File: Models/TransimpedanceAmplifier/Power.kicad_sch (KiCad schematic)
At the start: 4 parts

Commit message: Save progress
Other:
- note added: "TODO: Purchase links for regulators Purchase links for new trimpots (Y variant) Footprints for 0805 capacitors Purchase links & footprints for Schottky diodes Finalize all decoupling networks"
- note removed: "TODO: Purchase links for regulators Purchase links for new trimpots (Y variant)"
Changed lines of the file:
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@@
 		)
 	)
-	(text "TODO:\nPurchase links for regulators\nPurchase links for new trimpots (Y variant)"
+	(text "TODO:\nPurchase links for regulators\nPurchase links for new trimpots (Y variant)\nFootprints for 0805 capacitors\nPurchase links & footprints for Schottky diodes\nFinalize all decoupling networks"
 		(exclude_from_sim no)
-		(at 107.442 61.976 0)
+		(at 102.616 56.896 0)
 		(effects
 			(font

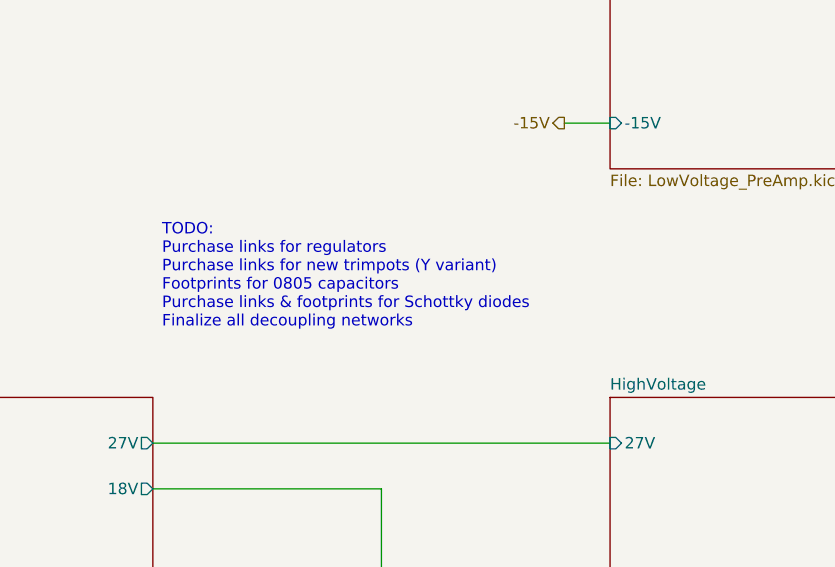
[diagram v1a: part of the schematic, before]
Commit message: Overhauled the purchase links for regulators and trimpots
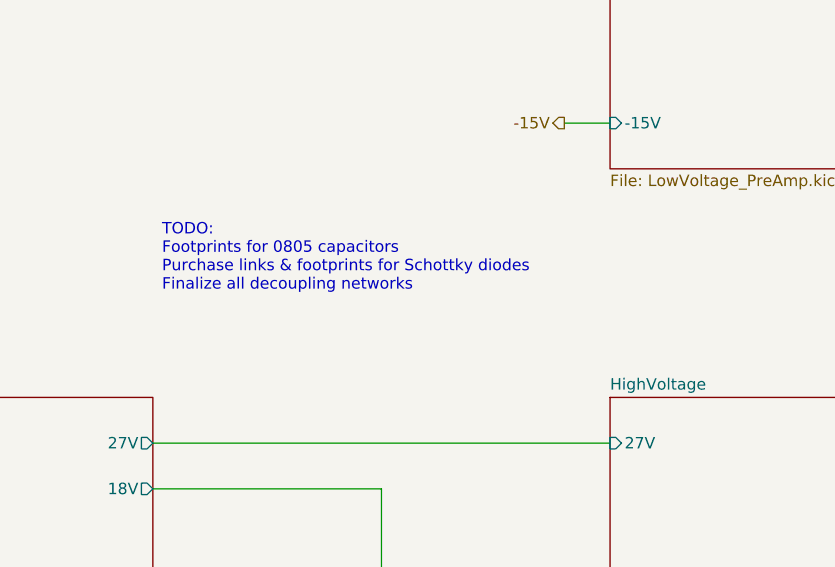
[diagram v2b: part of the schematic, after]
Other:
- note added: "TODO: Footprints for 0805 capacitors Purchase links & footprints for Schottky diodes Finalize all decoupling networks"
- note removed: "TODO: Purchase links for regulators Purchase links for new trimpots (Y variant) Footprints for 0805 capacitors Purchase links & footprints for Schottky diodes Finalize all decoupling networks"
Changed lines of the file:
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@@
 		)
 	)
-	(text "TODO:\nPurchase links for regulators\nPurchase links for new trimpots (Y variant)\nFootprints for 0805 capacitors\nPurchase links & footprints for Schottky diodes\nFinalize all decoupling networks"
+	(text "TODO:\nFootprints for 0805 capacitors\nPurchase links & footprints for Schottky diodes\nFinalize all decoupling networks"
 		(exclude_from_sim no)
 		(at 102.616 56.896 0)

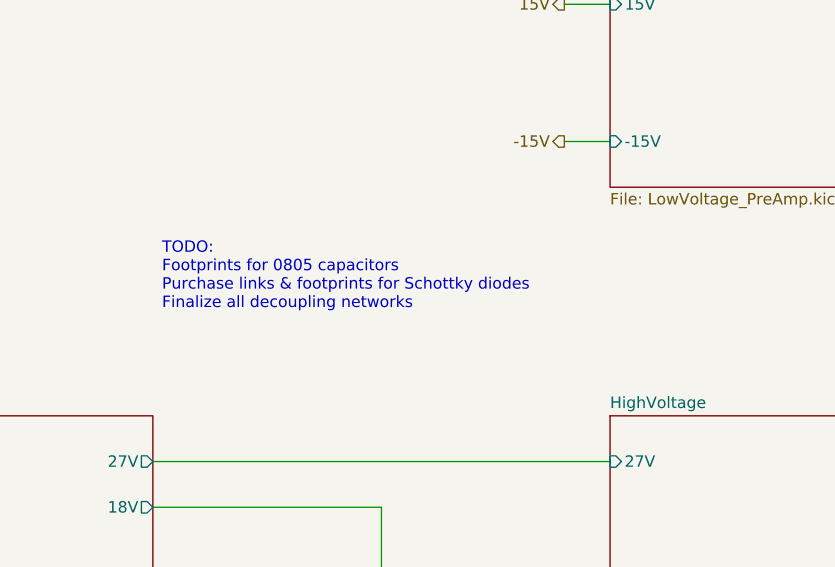
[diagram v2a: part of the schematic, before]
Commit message: Finished the footprint for 0805 capacitors
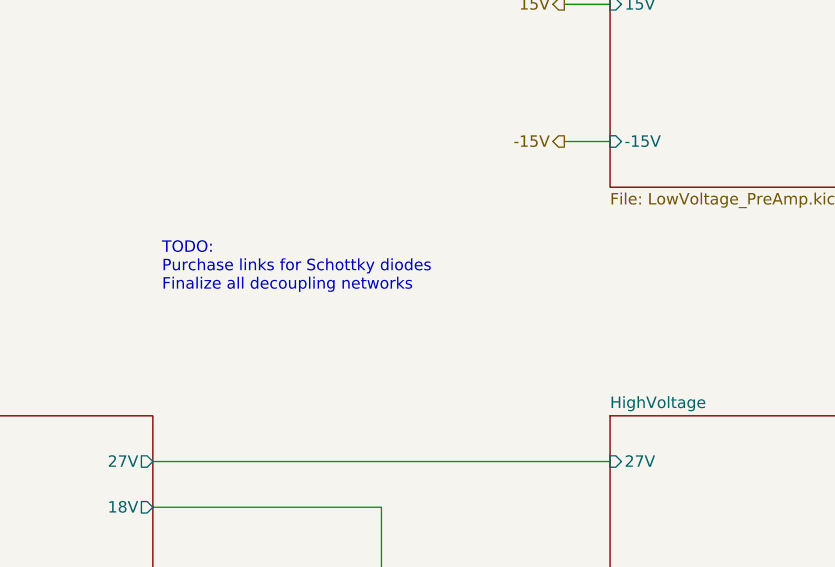
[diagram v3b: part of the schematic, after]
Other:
- note added: "TODO: Purchase links for Schottky diodes Finalize all decoupling networks"
- note removed: "TODO: Footprints for 0805 capacitors Purchase links & footprints for Schottky diodes Finalize all decoupling networks"
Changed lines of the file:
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@@
 		)
 	)
-	(text "TODO:\nFootprints for 0805 capacitors\nPurchase links & footprints for Schottky diodes\nFinalize all decoupling networks"
+	(text "TODO:\nPurchase links for Schottky diodes\nFinalize all decoupling networks"
 		(exclude_from_sim no)
 		(at 102.616 56.896 0)

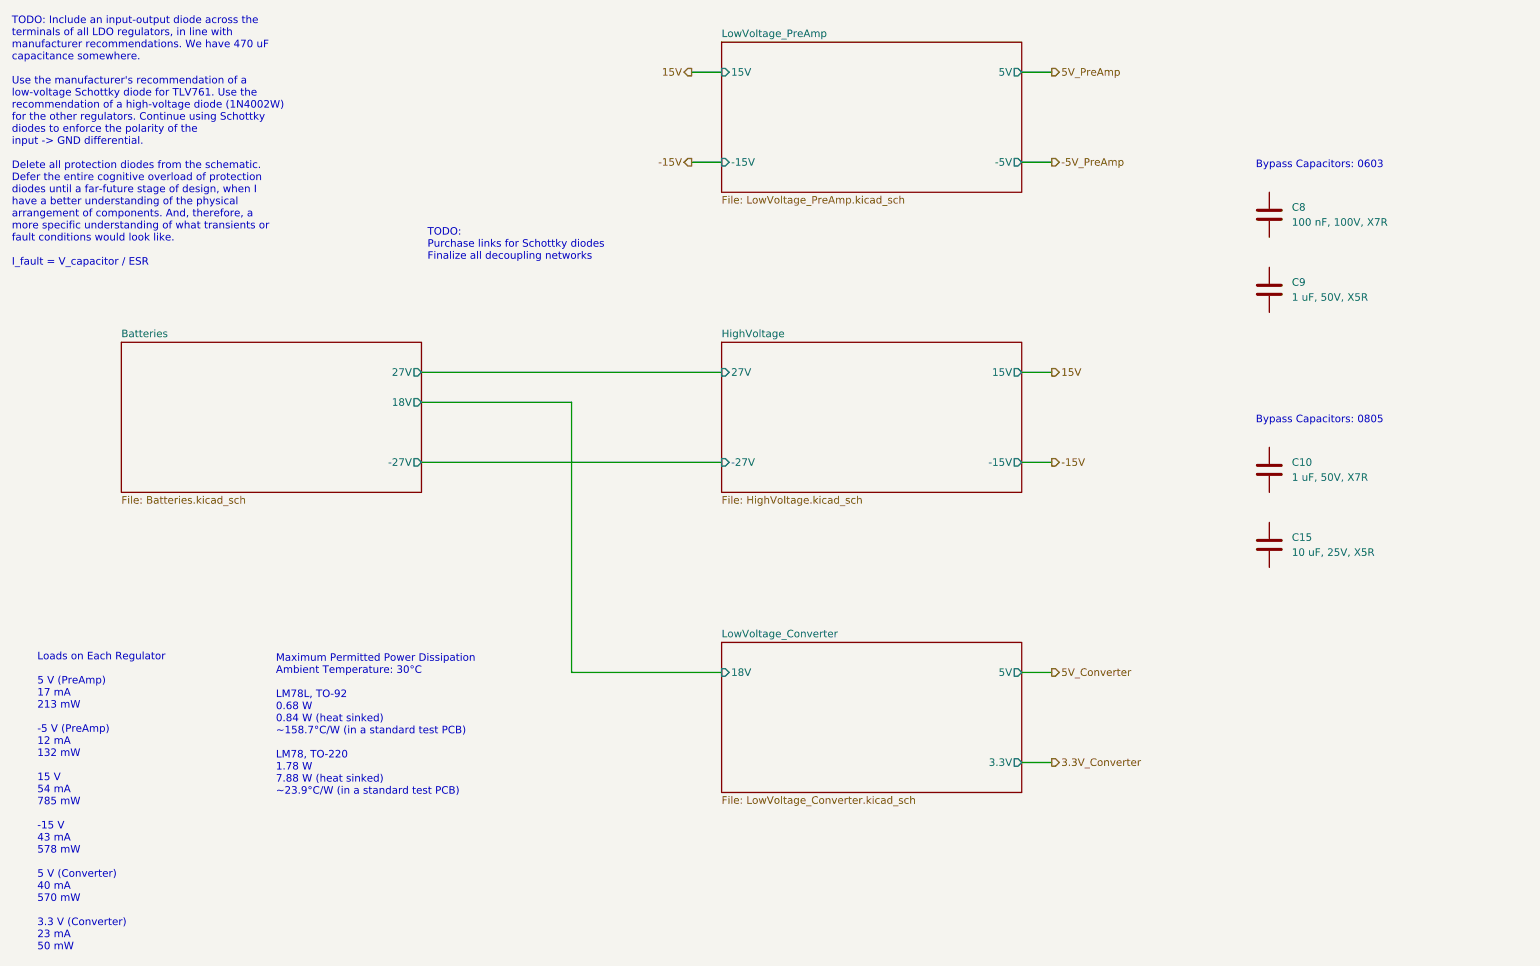
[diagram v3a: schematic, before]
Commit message: Now have all the purchase links for decoupling network components
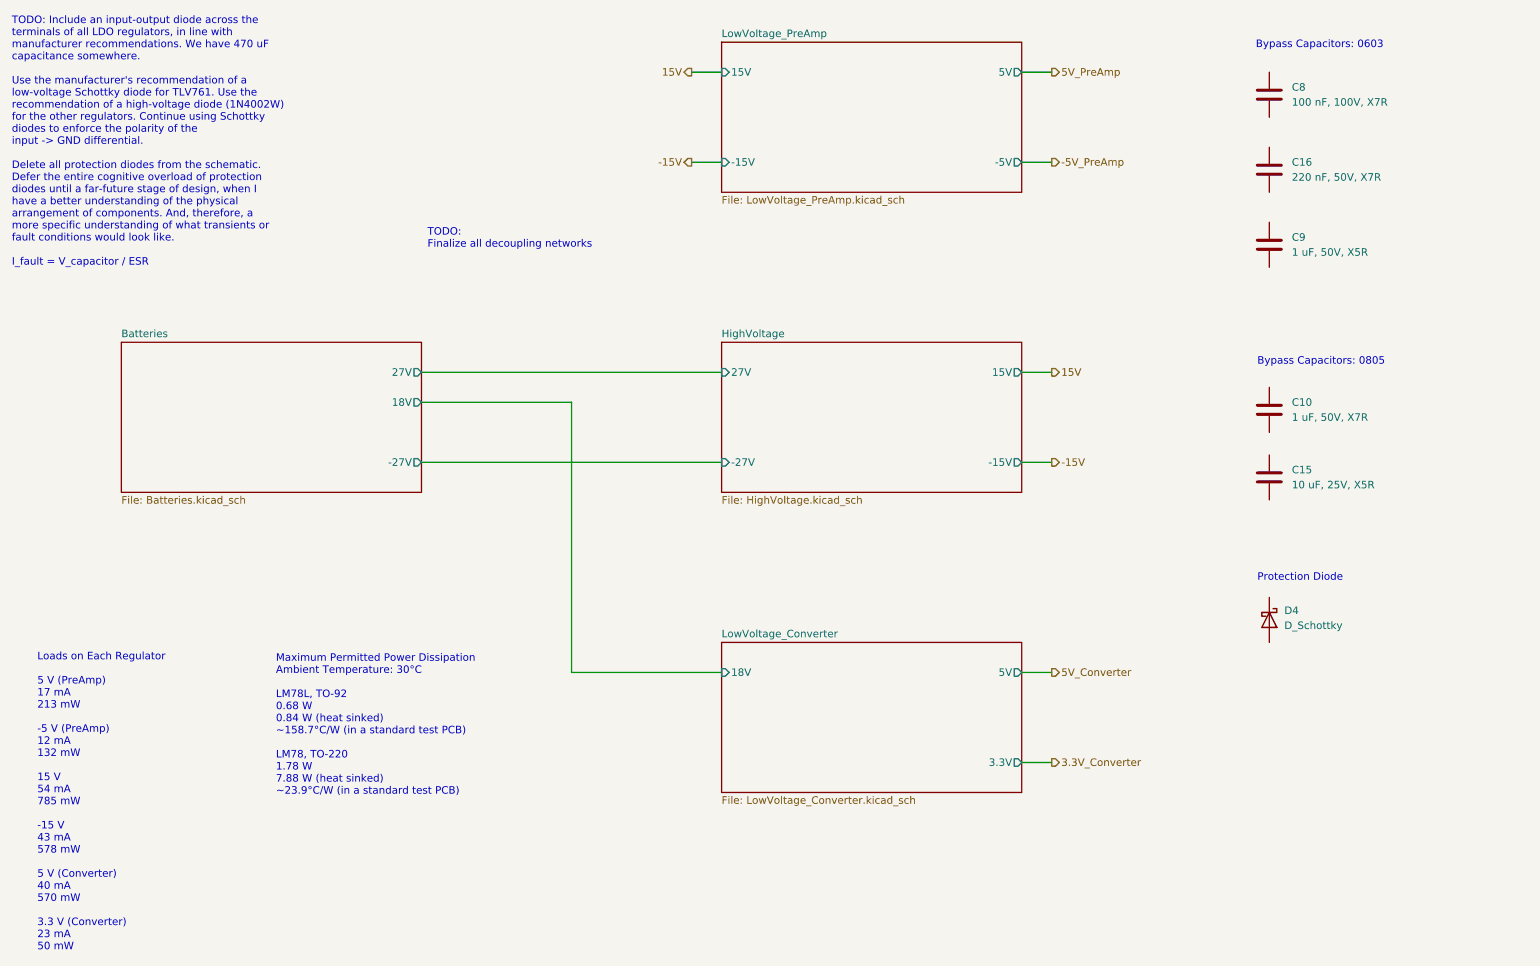
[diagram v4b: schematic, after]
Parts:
- added C16: 220 nF, 50V, X7R, symbol Device:C
- added D4: D_Schottky, symbol Device:D_Schottky
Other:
- note added: "Protection Diode"
- note added: "TODO: Finalize all decoupling networks"
- note removed: "TODO: Purchase links for Schottky diodes Finalize all decoupling networks"
- moved on the sheet: C10, C15, C8, C9
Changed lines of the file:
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@@
 		)
 	)
-	(text "TODO:\nPurchase links for Schottky diodes\nFinalize all decoupling networks"
+	(text "TODO:\nFinalize all decoupling networks"
 		(exclude_from_sim no)
 		(at 102.616 56.896 0)
@@
 	(text "Bypass Capacitors: 0805"
 		(exclude_from_sim no)
-		(at 242.824 88.646 0)
+		(at 243.078 78.74 0)
 		(effects
 			(font
@@
 		)
 	)
+	(text "Protection Diode"
+		(exclude_from_sim no)
+		(at 243.078 115.316 0)
+		(effects
+			(font
+				(size 1.27 1.27)
+			)
+			(justify left top)
+		)
+	)
 	(text "Maximum Permitted Power Dissipation\nAmbient Temperature: 30°C\n\nLM78L, TO-92\n0.68 W\n0.84 W (heat sinked)\n~158.7°C/W (in a standard test PCB)\n\nLM78, TO-220\n1.78 W\n7.88 W (heat sinked)\n~23.9°C/W (in a standard test PCB)"
 		(exclude_from_sim no)
@@
 	(text "Bypass Capacitors: 0603"
 		(exclude_from_sim no)
-		(at 242.824 45.466 0)
+		(at 242.824 25.146 0)
 		(effects
 			(font
@@
 	(symbol
 		(lib_id "Device:C")
-		(at 245.11 67.31 0)
+		(at 245.11 59.69 0)
 		(unit 1)
 		(exclude_from_sim no)
@@
 		(fields_autoplaced yes)
 		(property "Reference" "C9"
-			(at 248.92 66.0399 0)
+			(at 248.92 58.4199 0)
 			(effects
 				(font
@@
 		)
 		(property "Value" "1 uF, 50V, X5R"
-			(at 248.92 68.5799 0)
+			(at 248.92 60.9599 0)
 			(effects
 				(font
@@
 		)
 		(property "Footprint" ""
-			(at 246.0752 71.12 0)
+			(at 246.0752 63.5 0)
 			(effects
 				(font
@@
 		)
 		(property "Datasheet" "~"
-			(at 245.11 67.31 0)
+			(at 245.11 59.69 0)
 			(effects
 				(font
@@
 		)
 		(property "Description" "Unpolarized capacitor"
-			(at 245.11 67.31 0)
+			(at 245.11 59.69 0)
 			(effects
 				(font
@@
 		)
 		(property "Purchase Link" "https://www.digikey.com/en/products/detail/murata-electronics/GRT188R61H105KE13D/5416752"
-			(at 245.11 67.31 0)
+			(at 245.11 59.69 0)
 			(effects
 				(font
@@
 	(symbol
 		(lib_id "Device:C")
-		(at 245.11 110.49 0)
+		(at 245.11 99.06 0)
 		(unit 1)
 		(exclude_from_sim no)
@@
 		(fields_autoplaced yes)
 		(property "Reference" "C15"
-			(at 248.92 109.2199 0)
+			(at 248.92 97.7899 0)
 			(effects
 				(font
@@
 		)
 		(property "Value" "10 uF, 25V, X5R"
-			(at 248.92 111.7599 0)
+			(at 248.92 100.3299 0)
 			(effects
 				(font
@@
 		)
 		(property "Footprint" ""
-			(at 246.0752 114.3 0)
+			(at 246.0752 102.87 0)
 			(effects
 				(font
@@
 		)
 		(property "Datasheet" "~"
-			(at 245.11 110.49 0)
+			(at 245.11 99.06 0)
 			(effects
 				(font
@@
 		)
 		(property "Description" "Unpolarized capacitor"
-			(at 245.11 110.49 0)
+			(at 245.11 99.06 0)
 			(effects
 				(font
@@
 		)
 		(property "Purchase Link" "https://www.digikey.com/en/products/detail/murata-electronics/GRM21BR61E106KA73K/4905532"
-			(at 245.11 110.49 0)
+			(at 245.11 99.06 0)
 			(effects
 				(font
@@
 	)
 	(symbol
+		(lib_id "Device:D_Schottky")
+		(at 245.11 123.19 270)
+		(unit 1)
+		(exclude_from_sim no)
+		(in_bom yes)
+		(on_board yes)
+		(dnp no)
+		(fields_autoplaced yes)
+		(property "Reference" "D4"
+			(at 247.65 121.6024 90)
+			(effects
+				(font
+					(size 1.27 1.27)
+				)
+				(justify left)
+			)
+		)
+		(property "Value" "D_Schottky"
+			(at 247.65 124.1424 90)
+			(effects
+				(font
+					(size 1.27 1.27)
+				)
+				(justify left)
+			)
+		)
+		(property "Footprint" ""
+			(at 245.11 123.19 0)
+			(effects
+				(font
+					(size 1.27 1.27)
+				)
+				(hide yes)
+			)
+		)
+		(property "Datasheet" "~"
+			(at 245.11 123.19 0)
+			(effects
+				(font
+					(size 1.27 1.27)
+				)
+				(hide yes)
+			)
+		)
+		(property "Description" "Schottky diode"
+			(at 245.11 123.19 0)
+			(effects
+				(font
+					(size 1.27 1.27)
+				)
+				(hide yes)
+			)
+		)
+		(property "Purchase Link" "https://www.digikey.com/en/products/detail/diodes-incorporated/1N5819HW-7-F/814970"
+			(at 245.11 123.19 0)
+			(effects
+				(font
+					(size 1.27 1.27)
+				)
+				(hide yes)
+			)
+		)
+		(pin "2"
+		)
+		(pin "1"
+		)
+		(instances
+			(project ""
+				(path "/ec9f2ae3-e40d-40eb-9760-2b611ee8efd1/d0ece2d4-5b22-4822-ad0c-e2361683ec3d"
+					(reference "D4")
+					(unit 1)
+				)
+			)
+		)
+	)
+	(symbol
 		(lib_id "Device:C")
-		(at 245.11 54.61 0)
+		(at 245.11 46.99 0)
+		(unit 1)
+		(exclude_from_sim no)
+		(in_bom yes)
+		(on_board yes)
+		(dnp no)
+		(fields_autoplaced yes)
+		(property "Reference" "C16"
+			(at 248.92 45.7199 0)
+			(effects
+				(font
+					(size 1.27 1.27)
+				)
+				(justify left)
+			)
+		)
+		(property "Value" "220 nF, 50V, X7R"
+			(at 248.92 48.2599 0)
+			(effects
+				(font
+					(size 1.27 1.27)
+				)
+				(justify left)
+			)
+		)
+		(property "Footprint" ""
+			(at 246.0752 50.8 0)
+			(effects
+				(font
+					(size 1.27 1.27)
+				)
+				(hide yes)
+			)
+		)
+		(property "Datasheet" "~"
+			(at 245.11 46.99 0)
+			(effects
+				(font
+					(size 1.27 1.27)
+				)
+				(hide yes)
+			)
+		)
+		(property "Description" "Unpolarized capacitor"
+			(at 245.11 46.99 0)
+			(effects
+				(font
+					(size 1.27 1.27)
+				)
+				(hide yes)
+			)
+		)
+		(property "Purchase Link" "https://www.digikey.com/en/products/detail/murata-electronics/GRM188R71H224KAC4D/5797498"
+			(at 245.11 46.99 0)
+			(effects
+				(font
+					(size 1.27 1.27)
+				)
+				(hide yes)
+			)
+		)
+		(pin "1"
+		)
+		(pin "2"
+		)
+		(instances
+			(project ""
+				(path "/ec9f2ae3-e40d-40eb-9760-2b611ee8efd1/d0ece2d4-5b22-4822-ad0c-e2361683ec3d"
+					(reference "C16")
+					(unit 1)
+				)
+			)
+		)
+	)
+	(symbol
+		(lib_id "Device:C")
+		(at 245.11 34.29 0)
 		(unit 1)
 		(exclude_from_sim no)
@@
 		(fields_autoplaced yes)
 		(property "Reference" "C8"
-			(at 248.92 53.3399 0)
+			(at 248.92 33.0199 0)
 			(effects
 				(font
@@
 		)
 		(property "Value" "100 nF, 100V, X7R"
-			(at 248.92 55.8799 0)
+			(at 248.92 35.5599 0)
 			(effects
 				(font
@@
 		)
 		(property "Footprint" ""
-			(at 246.0752 58.42 0)
+			(at 246.0752 38.1 0)
 			(effects
 				(font
@@
 		)
 		(property "Datasheet" "~"
-			(at 245.11 54.61 0)
+			(at 245.11 34.29 0)
 			(effects
 				(font
@@
 		)
 		(property "Description" "Unpolarized capacitor"
-			(at 245.11 54.61 0)
+			(at 245.11 34.29 0)
 			(effects
 				(font
@@
 		)
 		(property "Purchase Link" "https://www.digikey.com/en/products/detail/murata-electronics/GRM188R72A104KA35D/702549"
-			(at 245.11 54.61 0)
+			(at 245.11 34.29 0)
 			(effects
 				(font
@@
 	(symbol
 		(lib_id "Device:C")
-		(at 245.11 97.79 0)
+		(at 245.11 87.63 0)
 		(unit 1)
 		(exclude_from_sim no)
@@
 		(fields_autoplaced yes)
 		(property "Reference" "C10"
-			(at 248.92 96.5199 0)
+			(at 248.92 86.3599 0)
 			(effects
 				(font
@@
 		)
 		(property "Value" "1 uF, 50V, X7R"
-			(at 248.92 99.0599 0)
+			(at 248.92 88.8999 0)
 			(effects
 				(font
@@
 		)
 		(property "Footprint" ""
-			(at 246.0752 101.6 0)
+			(at 246.0752 91.44 0)
 			(effects
 				(font
@@
 		)
 		(property "Datasheet" "~"
-			(at 245.11 97.79 0)
+			(at 245.11 87.63 0)
 			(effects
 				(font
@@
 		)
 		(property "Description" "Unpolarized capacitor"
-			(at 245.11 97.79 0)
+			(at 245.11 87.63 0)
 			(effects
 				(font
@@
 		)
 		(property "Purchase Link" "https://www.digikey.com/en/products/detail/murata-electronics/GRT21BR71H105KE01L/10702345"
-			(at 245.11 97.79 0)
-			(effects
-				(font
+			(at 245.11 87.63 0)
+			(effects
+				(font

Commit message: Refactoring in progress
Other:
- note added: "TODO: Delete these reference items once finished with the decoupling networks"
- note removed: "TODO: Finalize all decoupling networks"
- note removed: "TODO: Include an input-output diode across the terminals of all LDO regulators, in line with manufacturer recommendations. We have 470 uF capacitance somewhere. Use the manufacturer's recommendation of a low-voltage Schottky diode for TLV761. Use the recommendation of a high-voltage diode (1N4002W) for the other regulators. Continue using Schottky diodes to enforce the polarity of the input -> GN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"
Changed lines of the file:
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@@
 	(generator_version "9.0")
 	(paper "A4")
-	(text "TODO: Include an input-output diode across the\nterminals of all LDO regulators, in line with\nmanufacturer recommendations. We have 470 uF\ncapacitance somewhere.\n\nUse the manufacturer's recommendation of a\nlow-voltage Schottky diode for TLV761. Use the\nrecommendation of a high-voltage diode (1N4002W)\nfor the other regulators. Continue using Schottky\ndiodes to enforce the polarity of the\ninput -> GND differential.\n\nDelete all protection diodes from the schematic.\nDefer the entire cognitive overload of protection\ndiodes until a far-future stage of design, when I\nhave a better understanding of the physical\narrangement of components. And, therefore, a\nmore specific understanding of what transients or\nfault conditions would look like.\n\nI_fault = V_capacitor / ESR"
-		(exclude_from_sim no)
-		(at 32.258 21.082 0)
-		(effects
-			(font
-				(size 1.27 1.27)
-			)
-			(justify left top)
-		)
-	)
-	(text "TODO:\nFinalize all decoupling networks"
-		(exclude_from_sim no)
-		(at 102.616 56.896 0)
-		(effects
-			(font
-				(size 1.27 1.27)
-			)
-			(justify left top)
-		)
-	)
 	(text "Loads on Each Regulator\n\n5 V (PreAmp)\n17 mA\n213 mW\n\n-5 V (PreAmp)\n12 mA\n132 mW\n\n15 V\n54 mA\n785 mW\n\n-15 V\n43 mA\n578 mW\n\n5 V (Converter)\n40 mA\n570 mW\n\n3.3 V (Converter)\n23 mA\n50 mW\n"
 		(exclude_from_sim no)
@@
 		(effects
 			(font
+				(size 1.27 1.27)
+			)
+			(justify left top)
+		)
+	)
+	(text "TODO: Delete these reference items\nonce finished with the decoupling networks"
+		(exclude_from_sim no)
+		(at 237.744 134.62 0)
+		(effects
+			(font

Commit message: Finished for today
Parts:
- removed C10: 1 uF, 50V, X7R, symbol Device:C
- removed C15: 10 uF, 25V, X5R, symbol Device:C
- removed C16: 220 nF, 50V, X7R, symbol Device:C
- removed C8: 100 nF, 100V, X7R, symbol Device:C
- removed C9: 1 uF, 50V, X5R, symbol Device:C
- removed D4: D_Schottky, symbol Device:D_Schottky
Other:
- note removed: "Bypass Capacitors: 0603"
- note removed: "Bypass Capacitors: 0805"
- note removed: "Protection Diode"
- note removed: "TODO: Delete these reference items once finished with the decoupling networks"
